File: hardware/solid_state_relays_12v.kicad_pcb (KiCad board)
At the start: 2 copper layers, 120 x 90 mm, 78 parts, among them J1 1190297, J2 1190297, J3 1190297, J4 1190297, J5 1190297, J6 1190297, J7 1190297, J8 1190297, Q1 IRF4905PBF, Q2 IRF4905PBF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

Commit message: WIP control connector changes
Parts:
- added #LOGO_CC: Symbol_CreativeCommons_SilkScreenTop_Type2_Big, Symbol:Symbol_CreativeCommons_SilkScreenTop_Type2_Big, F.Cu at (49.5, 70.0)
- added #LOGO_GITHUB_URL1: GitHub URL, LOGO, B.Cu at (80.0, 60.0)
- added #LOGO_KICAD1: KiCad-Logo2_5mm_SilkScreen, Symbol:KiCad-Logo2_5mm_SilkScreen, F.Cu at (77.5, 52.2)
- added #LOGO_OSHW1: OSHW-Logo_11.4x12mm_SilkScreen, Symbol:OSHW-Logo_11.4x12mm_SilkScreen, F.Cu at (53.5, 52.2)
- added FID1: Fiducial, Fiducial:Fiducial_0.5mm_Mask1mm, F.Cu at (20.0, 28.0)
- added FID2: Fiducial, Fiducial:Fiducial_0.5mm_Mask1mm, F.Cu at (130.0, 28.0)
- added FID3: Fiducial, Fiducial:Fiducial_0.5mm_Mask1mm, F.Cu at (130.0, 90.0)
- added JCNTL2: Conn_02x05_Odd_Even, dragon_mobile:PinHeader_2x05_P1.27mm_Vertical, F.Cu at (77.0, 88.7)
- added JPWR2: XT60PW-M, dragon_mobile:XT60PWM, F.Cu at (31.7, 71.5)
- HQ1, HQ2, HQ3, HQ4, HQ5, HQ6, HQ7, HQ8: value HeatsinkHole -> Access Hole; footprint MountingHole:MountingHole_3.2mm_M3_Pad_Via -> dragon_mobile:MountingHole_6.1mm_Pad_Via
- JCNTL1: value Conn_01x12 -> Conn_02x05_Odd_Even; footprint Connector_JST:JST_GH_SM12B-GHS-TB_1x12-1MP_P1.25mm_Horizontal -> dragon_mobile:PinHeader_2x05_P1.27mm_Vertical
- JP1: renamed from JP2; value Conn_01x02 -> SolderJumper_2_Bridged; footprint dragon_mobile:PinHeader_1x02_P1.00mm_Vertical -> Jumper:SolderJumper-2_P1.3mm_Bridged_RoundedPad1.0x1.5mm
- JP2: renamed from JP1; value SolderJumper_2_Bridged -> Conn_01x02; footprint Jumper:SolderJumper-2_P1.3mm_Bridged_RoundedPad1.0x1.5mm -> dragon_mobile:PinHeader_1x02_P1.00mm_Vertical
- R1, RL1, RL2, RL3, RL4, RL5, RL6, RL7, RL8: value 1k5 -> 680
- TVS1, TVS2, TVS3, TVS4, TVS5, TVS6, TVS7, TVS8, TVSP1, TVSP2: value SM6T30AY -> SM6T16V5AY
- moved LED8 91.5 mm to (124.2, 99.0)
- moved JL8 91.5 mm to (125.2, 96.0)
- moved RL8 91.5 mm to (124.2, 93.0)
- moved TVS8 91.5 mm to (124.2, 87.5)
- moved JL4 83.5 mm to (32.9, 24.0)
- moved LED4 83.5 mm to (33.9, 21.0)
- moved RL4 83.4 mm to (33.9, 27.0)
- moved TVS4 83.4 mm to (33.9, 32.5)
- moved HQ1 79.5 mm to (118.5, 53.0)
- moved J1 79.5 mm to (121.0, 30.2)
- moved Q1 79.5 mm to (121.1, 36.8)
- moved RP1 79.5 mm to (121.1, 40.4)
- moved Q8 73.1 mm to (112.0, 83.2)
- moved RP8 73.1 mm to (112.0, 79.7)
- moved J8 73.1 mm to (112.1, 89.8)
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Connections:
- JCNTL1 pad 1: +BATT -> /a1
- JCNTL1 pad 10: /a3 -> GNDPWR
- JCNTL1 pad 2: /a5 -> GNDPWR
- JCNTL1 pad 3: /a6 -> /a2
- JCNTL1 pad 4: /a7 -> GNDPWR
- JCNTL1 pad 5: /a8 -> /a4
- JCNTL1 pad 7: +BATT -> /a3
- JCNTL1 pad 8: /a1 -> GNDPWR
- JCNTL1 pad 9: /a2 -> +BATT
- JP1 pad 1: GNDPWR -> +BATT
- JP1 pad 2: Net-(JP2-Pad2) -> Net-(JP1-Pad2)
- JP2 pad 1: +BATT -> GNDPWR
- JP2 pad 2: Net-(JP1-Pad2) -> Net-(JP2-Pad2)
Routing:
- net /a7: track 77.2 -> 21.8 mm
- net /a8: track 100.2 -> 55.1 mm
- net /a5: track 29.3 -> 69.2 mm
- net /a3: track 49.6 -> 14.9 mm
- net /a4: track 26.6 -> 54.6 mm
- net /a1: track 97.6 -> 72.9 mm
- net /a2: track 74.6 -> 52.6 mm
- net +BATT: track 17.2 -> 3.22 mm, vias 93 -> 120
- net /a6: track 52.1 -> 48.1 mm
- net Net-(JL8-Pad2): track 5.30 -> 4.30 mm
- net Net-(JL6-Pad2): track 5.30 -> 4.30 mm
- net Net-(JL5-Pad2): track 5.30 -> 4.30 mm
- net Net-(JL4-Pad2): track 5.30 -> 4.30 mm
- net Net-(JL3-Pad2): track 5.30 -> 4.30 mm
- net Net-(JL2-Pad2): track 5.30 -> 4.30 mm
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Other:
- board text added: "6"
- board text added: "HQ1-8 Access / Transistor Mounting Holes"
- board text added: "JPWR1"
- board text added: "JPWR2"
- board text added: "Mounting Holes H1-3"
- board text added: "Mounting Holes H4-6"
- board text added: "Mounting holes (H1-6) are for M3 screws/bolts and should be drilled at 2.5mm (#39) and tapped at .5mm threads. WARNING: The tabs on the output transistors Q1-8 are at supply voltage and MUST BE electrically isolated from ground when mounting. The HQ1-8 transistor access holes are also based on M3 and should allow the top of a pan head to pass through but the actual mounting holes should be drille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"
- board text added: "OUT1"
- board text added: "OUT2"
- board text added: "OUT3"
- board text added: "OUT4"
- board text added: "OUT5"
- board text added: "OUT6"
- board text added: "OUT7"
- board text added: "OUT8"
- board text added: "Rev:0.0.6"
- board text added: "© 2022 Michael Cummings"

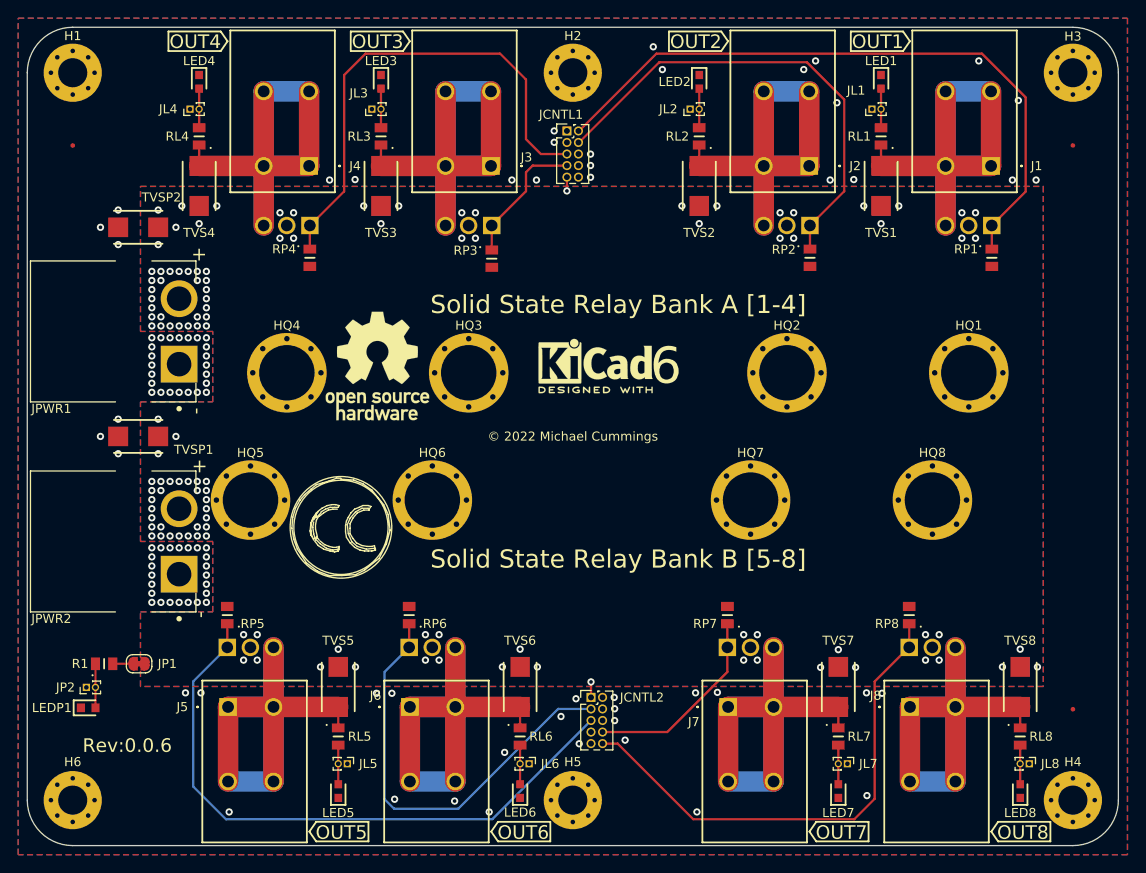
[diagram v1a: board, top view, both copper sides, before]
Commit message: Updated connectors and improved ground plane for control signals
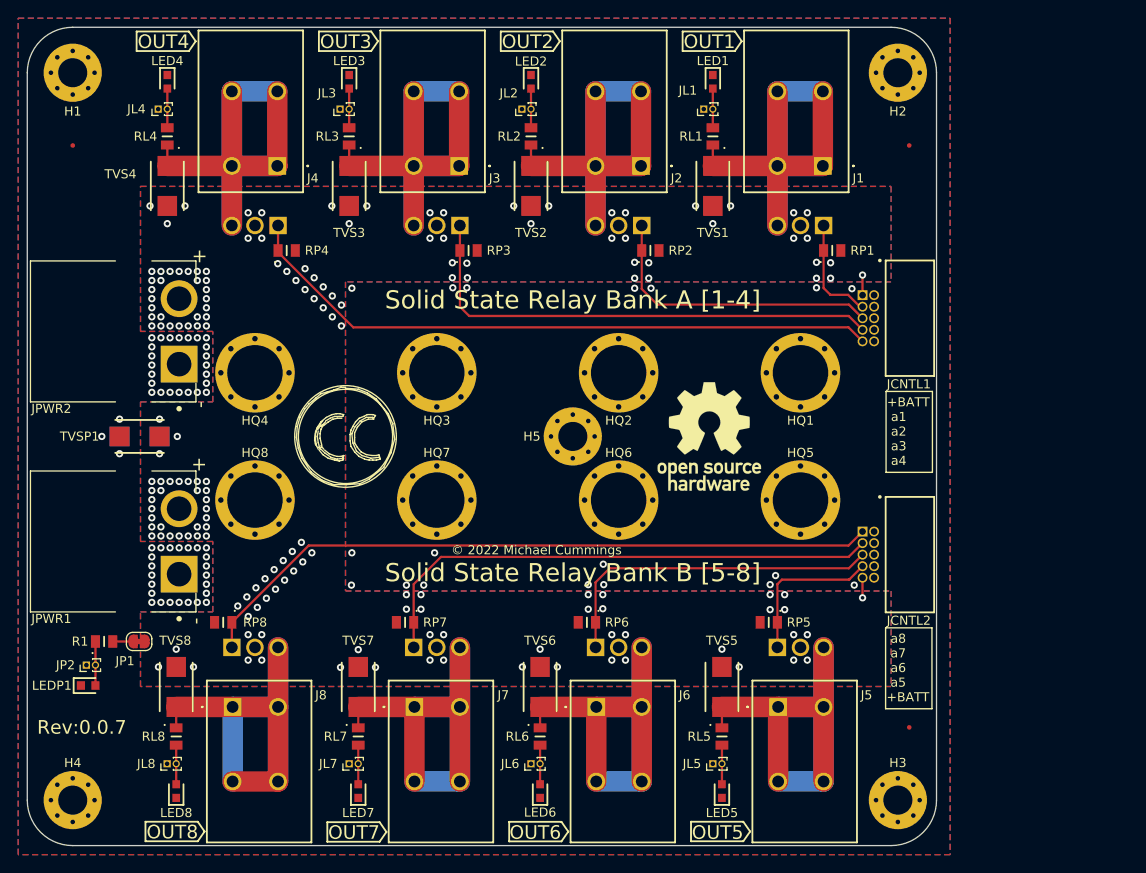
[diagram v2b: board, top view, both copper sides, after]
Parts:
- removed H6: MountingHole, MountingHole:MountingHole_3.2mm_M3_Pad_Via
- #LOGO_KICAD1, TVSP2: moved to B.Cu
- JCNTL1, JCNTL2: value Conn_02x05_Odd_Even -> SHF-105-01-L-D-RA; footprint dragon_mobile:PinHeader_2x05_P1.27mm_Vertical -> dragon_mobile:SAMTEC_SHF-105-01-L-D-RA
- moved H4 110.0 mm to (20.0, 100.0)
- moved JL8 94.8 mm to (30.4, 96.0), turned to 90 degrees
- moved LED8 92.8 mm to (31.4, 99.0)
- moved RL8 92.8 mm to (31.4, 93.0)
- moved TVS8 92.8 mm to (31.4, 87.5)
- moved H3 82.3 mm to (110.8, 100.0)
- moved RP8 75.5 mm to (36.5, 80.5), turned to 180 degrees
- moved HQ8 74.5 mm to (40.0, 67.0)
- moved J8 74.5 mm to (37.6, 89.8)
- moved Q8 74.5 mm to (37.5, 83.2)
- moved J5 60.5 mm to (97.6, 89.8)
- moved Q5 60.5 mm to (97.5, 83.2)
- moved HQ5 60.5 mm to (100.0, 67.0)
- moved RP5 59.6 mm to (96.5, 80.5), turned to 180 degrees
- moved JL7 54.8 mm to (50.4, 96.0), turned to 90 degrees
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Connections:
- HQ1 pad 1: +BATT -> GNDPWR
- HQ2 pad 1: +BATT -> GNDPWR
- HQ3 pad 1: +BATT -> GNDPWR
- HQ5 pad 1: +BATT -> GNDPWR
- HQ6 pad 1: +BATT -> GNDPWR
- HQ7 pad 1: +BATT -> GNDPWR
- JCNTL1 pad 1: /a1 -> +BATT
- JCNTL1 pad 3: /a2 -> /a1
- JCNTL1 pad 5: /a4 -> /a2
- JCNTL1 pad 9: +BATT -> /a4
- JCNTL2 pad 1: +BATT -> /a8
- JCNTL2 pad 10: /a8 -> GNDPWR
- JCNTL2 pad 3: /a6 -> /a7
- JCNTL2 pad 5: /a5 -> /a6
- JCNTL2 pad 7: GNDPWR -> /a5
- JCNTL2 pad 8: /a7 -> GNDPWR
- JCNTL2 pad 9: GNDPWR -> +BATT
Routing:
- net /a1: track 72.9 -> 11.7 mm
- net /a5: track 69.2 -> 17.1 mm
- net /a3: track 14.9 -> 54.3 mm
- net /a7: track 21.8 -> 58.2 mm
- net /a8: track 55.1 -> 76.3 mm
- net /a2: track 52.6 -> 32.6 mm
- net /a4: track 54.6 -> 71.1 mm
- net /a6: track 48.1 -> 37.8 mm
- net +BATT: track 3.22 -> 4.42 mm, vias 120 -> 169
- net OUT6: track 62.1 -> 61.2 mm
- net OUT5: track 62.1 -> 61.2 mm
- net OUT7: track 62.1 -> 61.2 mm
- net OUT8: track 62.1 -> 61.2 mm
- net GNDPWR: vias 96 -> 69
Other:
- board size 120 x 90 mm -> 100 x 90 mm
- board text added: "+BATT a1 a2 a3 a4"
- board text added: "0"
- board text added: "0 mm"
- board text added: "0.01 mm"
- board text added: "0.02"
- board text added: "0.07 mm"
- board text added: "1"
- board text added: "1 mm"
- board text added: "3.3"
- board text added: "4.5"
- board text added: "B.Cu"
- board text added: "B.Mask"
- board text added: "B.Paste"
- board text added: "B.Silkscreen"
- board text added: "Bottom Silk Screen"
- board text added: "Bottom Solder Mask"
- board text added: "Bottom Solder Paste"
- board text added: "Color"
- board text added: "Dielectric 1"
- board text added: "Epsilon R"
- board text added: "F.Cu"
- board text added: "F.Mask"
- board text added: "F.Paste"
- board text added: "F.Silkscreen"
- board text added: "FR4"
- board text added: "Green"
- board text added: "HQ1-4 Access Holes"
- board text added: "HQ5-8 Access Holes"
- board text added: "Layer Name"
- board text added: "Liquid Ink"
- board text added: "Liquid Photo"
- board text added: "Loss Tangent"
- board text added: "Material"
- board text added: "Mounting Holes H1-2"
- board text added: "Mounting Holes H3-4"
- board text added: "Mounting holes (H1-5) are for M3 screws/bolts and should be drilled at 2.5mm (#39) and tapped at .5mm threads. WARNING: The tabs on the output transistors Q1-8 are at supply voltage and MUST BE electrically isolated from ground when mounting. The HQ1-8 transistor access holes are also based on M3 and should allow the top of a pan head to pass through but the actual mounting holes should be drille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"
- board text added: "Rev:0.0.7"
- board text added: "Thickness (mm)"
- board text added: "Top Silk Screen"
- board text added: "Top Solder Mask"
- board text added: "Top Solder Paste"
- board text added: "Type"
- board text added: "White"
- board text added: "a8 a7 a6 a5 +BATT"
- board text added: "copper"
- board text added: "core"
- board text removed: "HQ1-8 Access / Transistor Mounting Holes"
- board text removed: "Mounting Holes H1-3"
- board text removed: "Mounting Holes H4-6"
- board text removed: "Mounting holes (H1-6) are for M3 screws/bolts and should be drilled at 2.5mm (#39) and tapped at .5mm threads. WARNING: The tabs on the output transistors Q1-8 are at supply voltage and MUST BE electrically isolated from ground when mounting. The HQ1-8 transistor access holes are also based on M3 and should allow the top of a pan head to pass through but the actual mounting holes should be drille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"
- board text removed: "Rev:0.0.6"
